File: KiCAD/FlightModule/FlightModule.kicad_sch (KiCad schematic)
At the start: 1 part, among them U1 ARDUINO_MKR_WAN_1310

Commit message: 本日の進捗をコミット
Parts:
- added Q1, Q2: AO3400A, Package_TO_SOT_SMD:SOT-23, symbol Transistor_FET:AO3400A
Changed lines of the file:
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@@
 	(paper "A4")
+	(symbol
+		(lib_id "Transistor_FET:AO3400A")
+		(at 167.64 40.64 0)
+		(unit 1)
+		(exclude_from_sim no)
+		(in_bom yes)
+		(on_board yes)
+		(dnp no)
+		(fields_autoplaced yes)
+		(property "Reference" "Q2"
+			(at 173.99 39.3699 0)
+			(effects
+				(font
+					(size 1.27 1.27)
+				)
+				(justify left)
+			)
+		)
+		(property "Value" "AO3400A"
+			(at 173.99 41.9099 0)
+			(effects
+				(font
+					(size 1.27 1.27)
+				)
+				(justify left)
+			)
+		)
+		(property "Footprint" "Package_TO_SOT_SMD:SOT-23"
+			(at 172.72 42.545 0)
+			(effects
+				(font
+					(size 1.27 1.27)
+					(italic yes)
+				)
+				(justify left)
+				(hide yes)
+			)
+		)
+		(property "Datasheet" "http://www.aosmd.com/pdfs/datasheet/AO3400A.pdf"
+			(at 172.72 44.45 0)
+			(effects
+				(font
+					(size 1.27 1.27)
+				)
+				(justify left)
+				(hide yes)
+			)
+		)
+		(property "Description" "30V Vds, 5.7A Id, N-Channel MOSFET, SOT-23"
+			(at 167.64 40.64 0)
+			(effects
+				(font
+					(size 1.27 1.27)
+				)
+				(hide yes)
+			)
+		)
+		(pin "1"
+		)
+		(pin "3"
+		)
+		(pin "2"
+		)
+		(instances
+			(project ""
+				(path "/3507137a-fdd7-4bc0-abe8-370b7c3b390e"
+					(reference "Q2")
+					(unit 1)
+				)
+			)
+		)
+	)
 	(symbol
 		(lib_id "ARDUINO_MKR_WAN_1310:ARDUINO_MKR_WAN_1310")
@@
 					(unit 1)
 				)
+			)
+		)
+	)
+	(symbol
+		(lib_id "Transistor_FET:AO3400A")
+		(at 166.37 63.5 0)
+		(unit 1)
+		(exclude_from_sim no)
+		(in_bom yes)
+		(on_board yes)
+		(dnp no)
+		(fields_autoplaced yes)
+		(property "Reference" "Q1"
+			(at 172.72 62.2299 0)
+			(effects
+				(font
+					(size 1.27 1.27)
+				)
+				(justify left)
+			)
+		)
+		(property "Value" "AO3400A"
+			(at 172.72 64.7699 0)
+			(effects
+				(font
+					(size 1.27 1.27)
+				)
+				(justify left)
+			)
+		)
+		(property "Footprint" "Package_TO_SOT_SMD:SOT-23"
+			(at 171.45 65.405 0)
+			(effects
+				(font
+					(size 1.27 1.27)
+					(italic yes)
+				)
+				(justify left)
+				(hide yes)
+			)
+		)
+		(property "Datasheet" "http://www.aosmd.com/pdfs/datasheet/AO3400A.pdf"
+			(at 171.45 67.31 0)
+			(effects
+				(font
+					(size 1.27 1.27)
+				)
+				(justify left)
+				(hide yes)
+			)
+		)
+		(property "Description" "30V Vds, 5.7A Id, N-Channel MOSFET, SOT-23"
+			(at 166.37 63.5 0)
+			(effects
+				(font
+					(size 1.27 1.27)
+				)
+				(hide yes)
+			)
+		)
+		(pin "3"
+		)
+		(pin "1"
+		)
+		(pin "2"
+		)
+		(instances
+			(project ""
+				(path "/3507137a-fdd7-4bc0-abe8-370b7c3b390e"
+					(reference "Q1")
+					(unit 1)
+				)

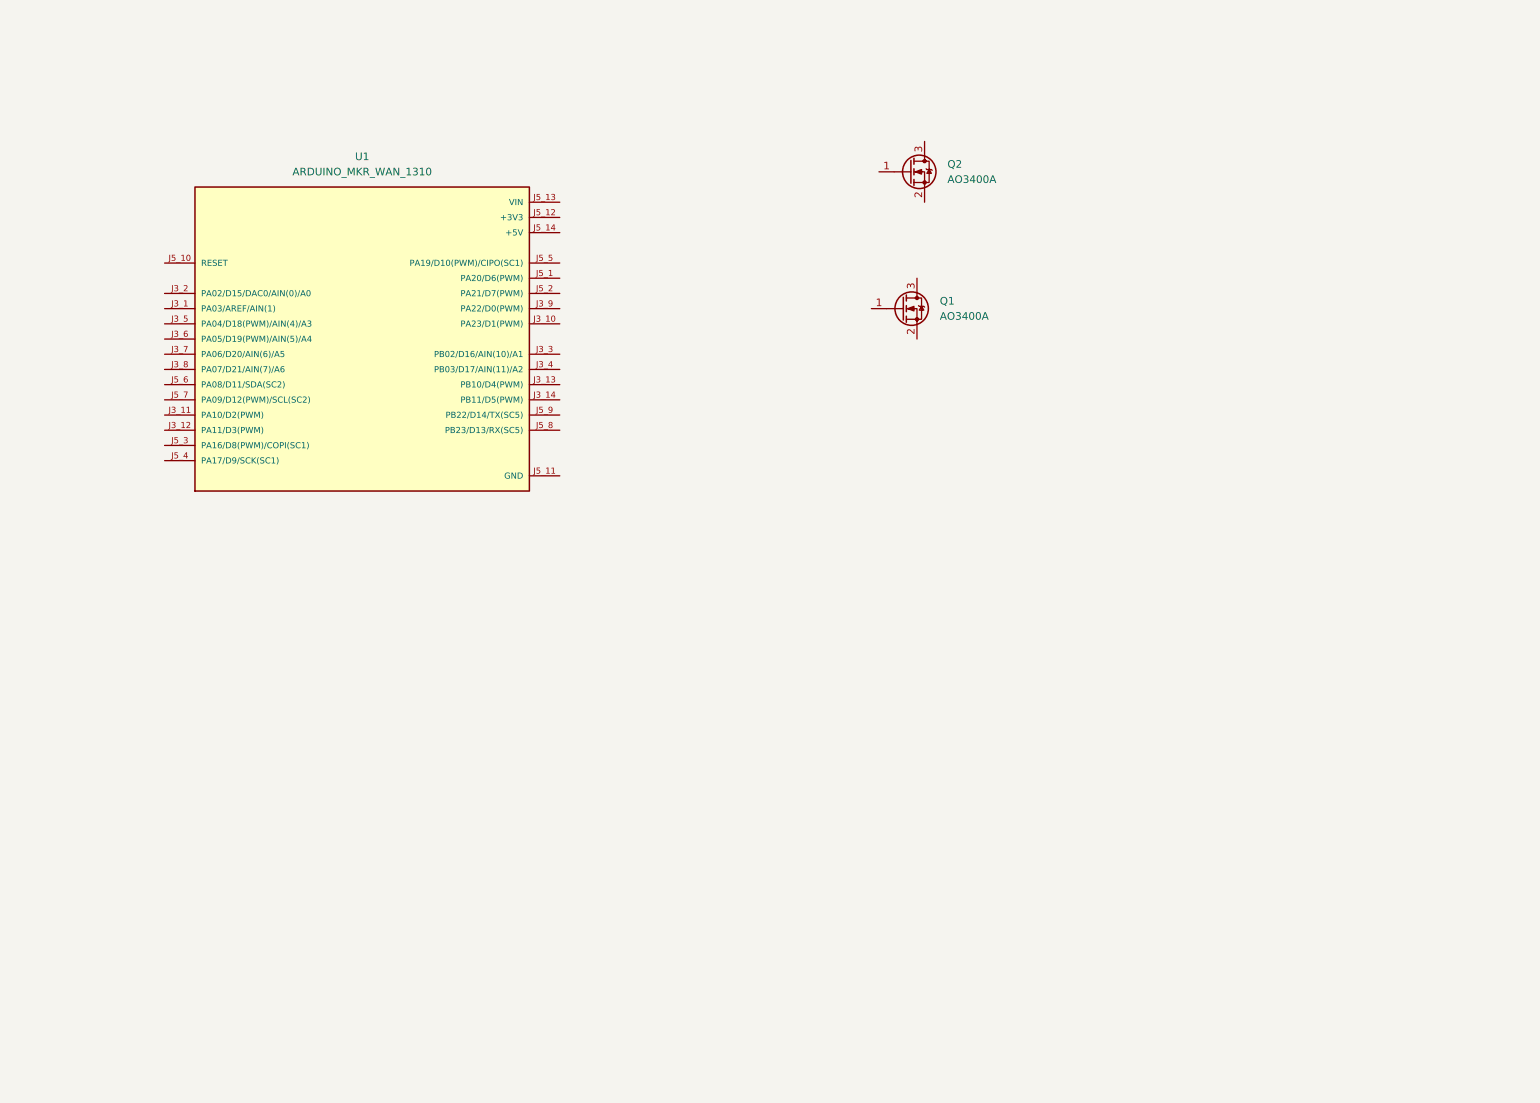
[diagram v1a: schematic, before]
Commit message: MB85RQ8MXを追加
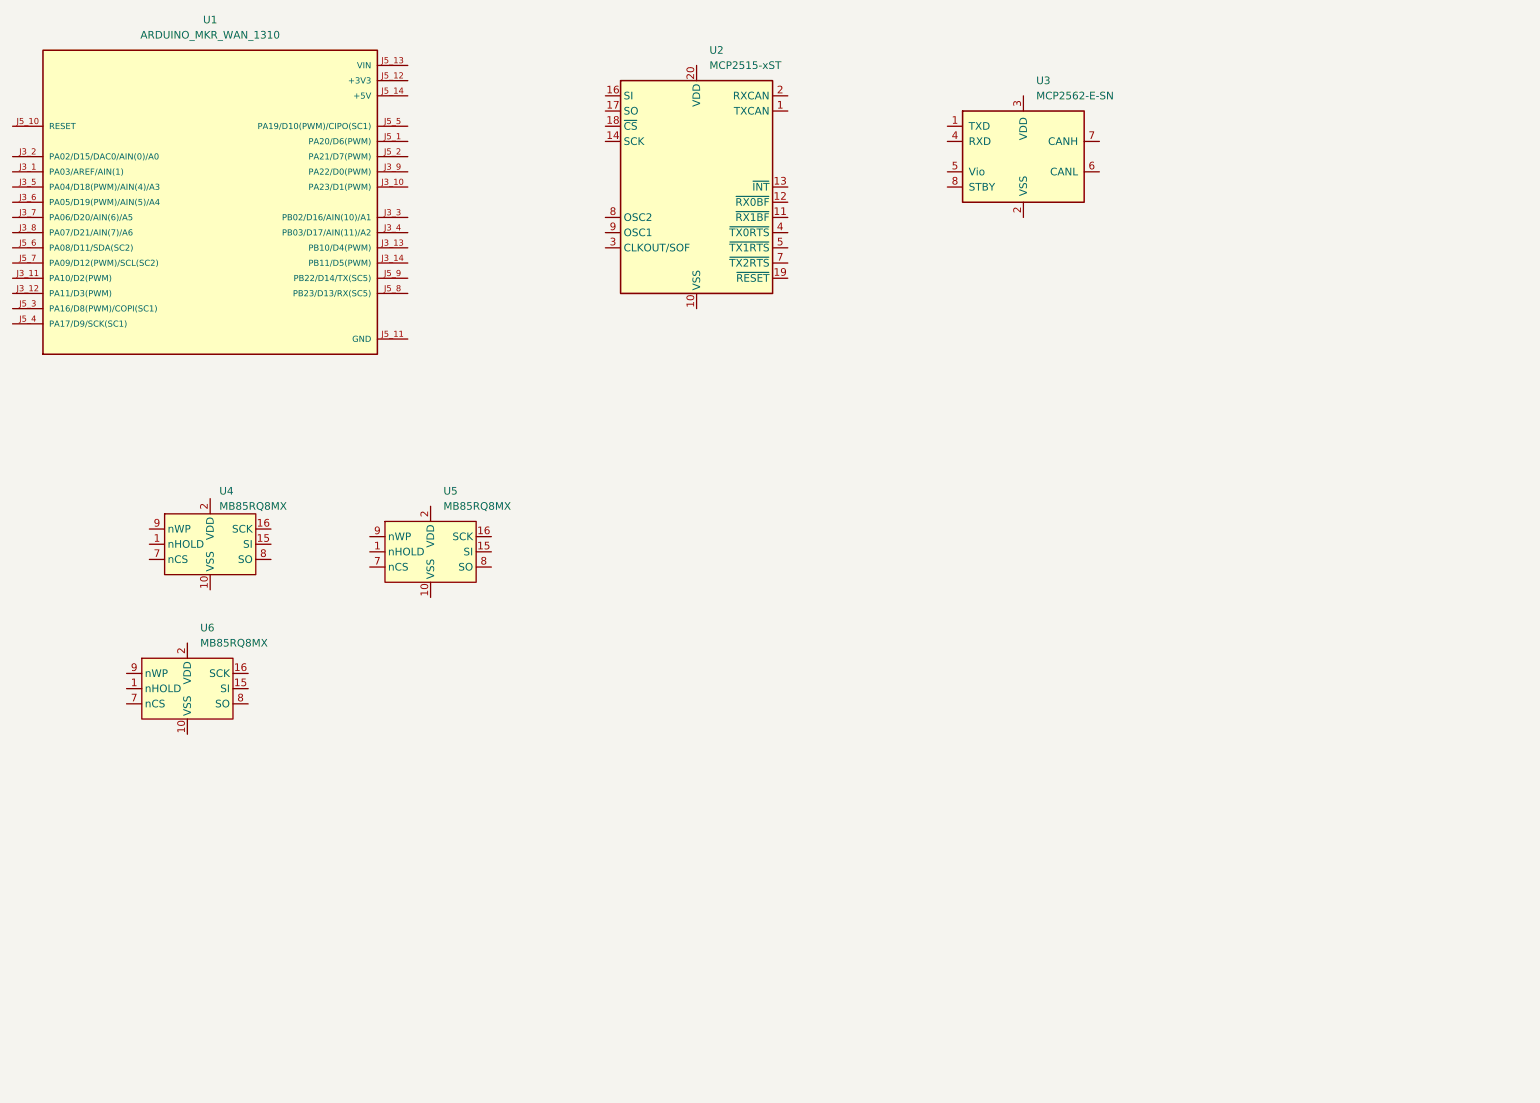
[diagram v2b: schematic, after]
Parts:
- removed Q1, Q2: AO3400A, Package_TO_SOT_SMD:SOT-23, symbol Transistor_FET:AO3400A
- added U2: MCP2515-xST, Package_SO:TSSOP-20_4.4x6.5mm_P0.65mm, symbol Interface_CAN_LIN:MCP2515-xST
- added U3: MCP2562-E-SN, Package_SO:SOIC-8_3.9x4.9mm_P1.27mm, symbol Interface_CAN_LIN:MCP2562-E-SN
- added U4: MB85RQ8MX, Package_SO:SOIC-16W_7.5x10.3mm_P1.27mm, symbol Memory_NVRAM:MB85RQ8MX
- added U5, U6: MB85RQ8MX, Package_SO:SOIC-16W_7.5x10.3mm_P1.27mm, symbol TSRP_IC:MB85RQ8MX

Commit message: 本日の進捗を保存
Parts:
- added U7: 74AHC1G14, symbol 74xGxx:74AHC1G14
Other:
- moved on the sheet: U4, U5, U6
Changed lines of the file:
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@@
 	(symbol
 		(lib_id "Memory_NVRAM:MB85RQ8MX")
-		(at 43.18 97.79 0)
+		(at 29.21 80.01 0)
 		(unit 1)
 		(exclude_from_sim no)
@@
 		(dnp no)
 		(property "Reference" "U4"
-			(at 52.324 93.98 0)
+			(at 38.354 76.2 0)
 			(effects
 				(font
@@
 		)
 		(property "Value" "MB85RQ8MX"
-			(at 52.324 96.52 0)
+			(at 38.354 78.74 0)
 			(effects
 				(font
@@
 		)
 		(property "Footprint" "Package_SO:SOIC-16W_7.5x10.3mm_P1.27mm"
-			(at 43.18 96.266 0)
+			(at 29.21 78.486 0)
 			(effects
 				(font
@@
 		)
 		(property "Datasheet" ""
-			(at 43.18 96.266 0)
+			(at 29.21 78.486 0)
 			(effects
 				(font
@@
 		)
 		(property "Description" ""
-			(at 43.18 96.266 0)
+			(at 29.21 78.486 0)
 			(effects
 				(font
@@
 		)
 		(property "Sim.Device" ""
-			(at 43.18 97.79 0)
+			(at 29.21 80.01 0)
 			(effects
 				(font
@@
 		)
 		(property "Sim.Pins" ""
-			(at 43.18 97.79 0)
+			(at 29.21 80.01 0)
 			(effects
 				(font
@@
 	)
 	(symbol
+		(lib_id "74xGxx:74AHC1G14")
+		(at 82.55 92.71 0)
+		(unit 1)
+		(exclude_from_sim no)
+		(in_bom yes)
+		(on_board yes)
+		(dnp no)
+		(fields_autoplaced yes)
+		(property "Reference" "U7"
+			(at 95.25 86.2898 0)
+			(effects
+				(font
+					(size 1.27 1.27)
+				)
+			)
+		)
+		(property "Value" "74AHC1G14"
+			(at 95.25 88.8298 0)
+			(effects
+				(font
+					(size 1.27 1.27)
+				)
+			)
+		)
+		(property "Footprint" ""
+			(at 82.55 92.71 0)
+			(effects
+				(font
+					(size 1.27 1.27)
+				)
+				(hide yes)
+			)
+		)
+		(property "Datasheet" "https://www.ti.com/lit/ds/symlink/sn74lvc1g14.pdf"
+			(at 82.55 99.06 0)
+			(effects
+				(font
+					(size 1.27 1.27)
+				)
+				(justify left)
+				(hide yes)
+			)
+		)
+		(property "Description" "Single Schmitt NOT Gate, Low-Voltage CMOS"
+			(at 82.55 92.71 0)
+			(effects
+				(font
+					(size 1.27 1.27)
+				)
+				(hide yes)
+			)
+		)
+		(pin "2"
+		)
+		(pin "5"
+		)
+		(pin "1"
+		)
+		(pin "3"
+		)
+		(pin "4"
+		)
+		(instances
+			(project ""
+				(path "/3507137a-fdd7-4bc0-abe8-370b7c3b390e"
+					(reference "U7")
+					(unit 1)
+				)
+			)
+		)
+	)
+	(symbol
 		(lib_id "TSRP_IC:MB85RQ8MX")
-		(at 80.01 99.06 0)
+		(at 29.21 123.19 0)
 		(unit 1)
 		(exclude_from_sim no)
@@
 		(fields_autoplaced yes)
 		(property "Reference" "U5"
-			(at 89.7733 93.98 0)
+			(at 38.9733 118.11 0)
 			(effects
 				(font
@@
 		)
 		(property "Value" "MB85RQ8MX"
-			(at 89.7733 96.52 0)
+			(at 38.9733 120.65 0)
 			(effects
 				(font
@@
 		)
 		(property "Footprint" "Package_SO:SOIC-16W_7.5x10.3mm_P1.27mm"
-			(at 80.01 97.536 0)
+			(at 29.21 121.666 0)
 			(effects
 				(font
@@
 		)
 		(property "Datasheet" ""
-			(at 80.01 97.536 0)
+			(at 29.21 121.666 0)
 			(effects
 				(font
@@
 		)
 		(property "Description" ""
-			(at 80.01 97.536 0)
+			(at 29.21 121.666 0)
 			(effects
 				(font
@@
 		)
 		(property "Sim.Device" ""
-			(at 80.01 99.06 0)
+			(at 29.21 123.19 0)
 			(effects
 				(font
@@
 		)
 		(property "Sim.Pins" ""
-			(at 80.01 99.06 0)
+			(at 29.21 123.19 0)
 			(effects
 				(font
@@
 	(symbol
 		(lib_id "TSRP_IC:MB85RQ8MX")
-		(at 39.37 121.92 0)
+		(at 29.21 102.87 0)
 		(unit 1)
 		(exclude_from_sim no)
@@
 		(fields_autoplaced yes)
 		(property "Reference" "U6"
-			(at 49.1333 116.84 0)
+			(at 38.9733 97.79 0)
 			(effects
 				(font
@@
 		)
 		(property "Value" "MB85RQ8MX"
-			(at 49.1333 119.38 0)
+			(at 38.9733 100.33 0)
 			(effects
 				(font
@@
 		)
 		(property "Footprint" "Package_SO:SOIC-16W_7.5x10.3mm_P1.27mm"
-			(at 39.37 120.396 0)
+			(at 29.21 101.346 0)
 			(effects
 				(font
@@
 		)
 		(property "Datasheet" ""
-			(at 39.37 120.396 0)
+			(at 29.21 101.346 0)
 			(effects
 				(font
@@
 		)
 		(property "Description" ""
-			(at 39.37 120.396 0)
+			(at 29.21 101.346 0)
 			(effects
 				(font
@@
 		)
 		(property "Sim.Device" ""
-			(at 39.37 121.92 0)
+			(at 29.21 102.87 0)
 			(effects
 				(font
@@
 		)
 		(property "Sim.Pins" ""
-			(at 39.37 121.92 0)
-			(effects
-				(font
+			(at 29.21 102.87 0)
+			(effects
+				(font

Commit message: 大型の部品を配置
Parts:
- added D1, D3: G, LED_SMD:LED_0603_1608Metric_Pad1.05x0.95mm_HandSolder, symbol Device:LED_Small
- added D2, D4: GS1010FL, Diode_SMD:D_SOD-123F, symbol Device:D_Small
- added Q1, Q2: AO3400A, Package_TO_SOT_SMD:SOT-23, symbol Transistor_FET:AO3400A
- added R1, R4: 300R, Resistor_SMD:R_0603_1608Metric_Pad0.98x0.95mm_HandSolder, symbol Device:R_Small
- added R2, R5: 10kR, Resistor_SMD:R_0603_1608Metric_Pad0.98x0.95mm_HandSolder, symbol Device:R_Small
- added R3, R6: 2.4kR, Resistor_SMD:R_0603_1608Metric_Pad0.98x0.95mm_HandSolder, symbol Device:R_Small
- added U8: L7805, symbol Regulator_Linear:L7805
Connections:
- new net: D3.1 (K), D4.2 (A), Q2.3 (D)
- new net: D3.2 (A), R6.2
- new net: Q1.1 (G), R1.2, R2.2
- new net: Q2.1 (G), R4.2, R5.2
- new net: D1.2 (A), R3.2
- new net: D1.1 (K), D2.2 (A), Q1.3 (D)
- new net +12V: D2.1 (K), D4.1 (K), R3.1, R6.1
- new net GND: Q1.2 (S), Q2.2 (S), R2.1, R5.1

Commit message: GPSSheildのフットプリントを救出
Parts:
- added IC1: ~, MKRGPSShield_V4.0:UBLOXLIB_SAM-M8Q, symbol MKRGPSShield_V4.0-eagle-import:SAM-M8Q
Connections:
- new net: IC1.1 (GND), IC1.10 (GND), IC1.11 (GND), IC1.15 (GND), IC1.16 (GND), IC1.20 (GND), IC1.4 (GND), IC1.5 (GND), IC1.6 (GND)
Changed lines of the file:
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@@
+	)
+	(symbol
+		(lib_id "MKRGPSShield_V4.0-eagle-import:SAM-M8Q")
+		(at 82.55 154.94 0)
+		(unit 1)
+		(exclude_from_sim no)
+		(in_bom yes)
+		(on_board yes)
+		(dnp no)
+		(fields_autoplaced yes)
+		(property "Reference" "IC1"
+			(at 82.55 154.94 0)
+			(effects
+				(font
+					(size 1.27 1.27)
+				)
+				(hide yes)
+			)
+		)
+		(property "Value" "~"
+			(at 82.55 154.94 0)
+			(effects
+				(font
+					(size 1.27 1.27)
+				)
+				(hide yes)
+			)
+		)
+		(property "Footprint" "MKRGPSShield_V4.0:UBLOXLIB_SAM-M8Q"
+			(at 82.55 154.94 0)
+			(effects
+				(font
+					(size 1.27 1.27)
+				)
+				(hide yes)
+			)
+		)
+		(property "Datasheet" ""
+			(at 82.55 154.94 0)
+			(effects
+				(font
+					(size 1.27 1.27)
+				)
+				(hide yes)
+			)
+		)
+		(property "Description" "u-blox SAM GNSS antenna module"
+			(at 82.55 154.94 0)
+			(effects
+				(font
+					(size 1.27 1.27)
+				)
+				(hide yes)
+			)
+		)
+		(pin "14"
+		)
+		(pin "13"
+		)
+		(pin "8"
+		)
+		(pin "17"
+		)
+		(pin "9"
+		)
+		(pin "12"
+		)
+		(pin "19"
+		)
+		(pin "7"
+		)
+		(pin "18"
+		)
+		(pin "2"
+		)
+		(pin "3"
+		)
+		(pin "1"
+		)
+		(pin "10"
+		)
+		(pin "11"
+		)
+		(pin "15"
+		)
+		(pin "16"
+		)
+		(pin "20"
+		)
+		(pin "4"
+		)
+		(pin "5"
+		)
+		(pin "6"
+		)
+		(instances
+			(project ""
+				(path "/3507137a-fdd7-4bc0-abe8-370b7c3b390e"
+					(reference "IC1")
+					(unit 1)
+				)
+			)
+		)
 	)
 	(symbol

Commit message: GPSShieldのフットプリントをFlightModuleに移植（手作業☠️）
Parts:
- IC1: footprint MKRGPSShield_V4.0:UBLOXLIB_SAM-M8Q -> GPSShield:UBLOXLIB_SAM-M8Q
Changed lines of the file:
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@@
+	)
+	(symbol
+		(lib_id "MKRGPSShield_V4.0-eagle-import:SAM-M8Q")
+		(at 81.28 162.56 0)
+		(unit 1)
+		(exclude_from_sim no)
+		(in_bom yes)
+		(on_board yes)
+		(dnp no)
+		(fields_autoplaced yes)
+		(property "Reference" "IC1"
+			(at 81.28 162.56 0)
+			(effects
+				(font
+					(size 1.27 1.27)
+				)
+				(hide yes)
+			)
+		)
+		(property "Value" "~"
+			(at 81.28 162.56 0)
+			(effects
+				(font
+					(size 1.27 1.27)
+				)
+				(hide yes)
+			)
+		)
+		(property "Footprint" "GPSShield:UBLOXLIB_SAM-M8Q"
+			(at 81.28 162.56 0)
+			(effects
+				(font
+					(size 1.27 1.27)
+				)
+				(hide yes)
+			)
+		)
+		(property "Datasheet" ""
+			(at 81.28 162.56 0)
+			(effects
+				(font
+					(size 1.27 1.27)
+				)
+				(hide yes)
+			)
+		)
+		(property "Description" "u-blox SAM GNSS antenna module"
+			(at 81.28 162.56 0)
+			(effects
+				(font
+					(size 1.27 1.27)
+				)
+				(hide yes)
+			)
+		)
+		(pin "11"
+		)
+		(pin "2"
+		)
+		(pin "15"
+		)
+		(pin "1"
+		)
+		(pin "3"
+		)
+		(pin "10"
+		)
+		(pin "8"
+		)
+		(pin "18"
+		)
+		(pin "16"
+		)
+		(pin "7"
+		)
+		(pin "5"
+		)
+		(pin "20"
+		)
+		(pin "19"
+		)
+		(pin "4"
+		)
+		(pin "6"
+		)
+		(pin "12"
+		)
+		(pin "13"
+		)
+		(pin "14"
+		)
+		(pin "17"
+		)
+		(pin "9"
+		)
+		(instances
+			(project ""
+				(path "/3507137a-fdd7-4bc0-abe8-370b7c3b390e"
+					(reference "IC1")
+					(unit 1)
+				)
+			)
+		)
 	)
 	(symbol
@@
 					(unit 1)
 				)
-			)
-		)
-	)
-	(symbol
-		(lib_id "MKRGPSShield_V4.0-eagle-import:SAM-M8Q")
-		(at 82.55 154.94 0)
-		(unit 1)
-		(exclude_from_sim no)
-		(in_bom yes)
-		(on_board yes)
-		(dnp no)
-		(fields_autoplaced yes)
-		(property "Reference" "IC1"
-			(at 82.55 154.94 0)
-			(effects
-				(font
-					(size 1.27 1.27)
-				)
-				(hide yes)
-			)
-		)
-		(property "Value" "~"
-			(at 82.55 154.94 0)
-			(effects
-				(font
-					(size 1.27 1.27)
-				)
-				(hide yes)
-			)
-		)
-		(property "Footprint" "MKRGPSShield_V4.0:UBLOXLIB_SAM-M8Q"
-			(at 82.55 154.94 0)
-			(effects
-				(font
-					(size 1.27 1.27)
-				)
-				(hide yes)
-			)
-		)
-		(property "Datasheet" ""
-			(at 82.55 154.94 0)
-			(effects
-				(font
-					(size 1.27 1.27)
-				)
-				(hide yes)
-			)
-		)
-		(property "Description" "u-blox SAM GNSS antenna module"
-			(at 82.55 154.94 0)
-			(effects
-				(font
-					(size 1.27 1.27)
-				)
-				(hide yes)
-			)
-		)
-		(pin "14"
-		)
-		(pin "13"
-		)
-		(pin "8"
-		)
-		(pin "17"
-		)
-		(pin "9"
-		)
-		(pin "12"
-		)
-		(pin "19"
-		)
-		(pin "7"
-		)
-		(pin "18"
-		)
-		(pin "2"
-		)
-		(pin "3"
-		)
-		(pin "1"
-		)
-		(pin "10"
-		)
-		(pin "11"
-		)
-		(pin "15"
-		)
-		(pin "16"
-		)
-		(pin "20"
-		)
-		(pin "4"
-		)
-		(pin "5"
-		)
-		(pin "6"
-		)
-		(instances
-			(project ""
-				(path "/3507137a-fdd7-4bc0-abe8-370b7c3b390e"
-					(reference "IC1")
-					(unit 1)
-				)

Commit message: GPSShieldの配線の再現の途中
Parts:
- added U9: ~, MKRGPSShield_V4.0:SOT25, symbol MKRGPSShield_V4.0-eagle-import:AP2112K-3.3
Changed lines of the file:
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@@
+	)
+	(symbol
+		(lib_id "MKRGPSShield_V4.0-eagle-import:AP2112K-3.3")
+		(at 149.86 143.51 0)
+		(unit 1)
+		(exclude_from_sim no)
+		(in_bom yes)
+		(on_board yes)
+		(dnp no)
+		(fields_autoplaced yes)
+		(property "Reference" "U9"
+			(at 149.86 134.62 0)
+			(effects
+				(font
+					(size 1.778 1.5113)
+				)
+			)
+		)
+		(property "Value" "~"
+			(at 149.86 137.16 0)
+			(effects
+				(font
+					(size 1.778 1.5113)
+				)
+			)
+		)
+		(property "Footprint" "MKRGPSShield_V4.0:SOT25"
+			(at 149.86 143.51 0)
+			(effects
+				(font
+					(size 1.27 1.27)
+				)
+				(hide yes)
+			)
+		)
+		(property "Datasheet" ""
+			(at 149.86 143.51 0)
+			(effects
+				(font
+					(size 1.27 1.27)
+				)
+				(hide yes)
+			)
+		)
+		(property "Description" "IC REG LINEAR 3.3V 600mA SOT25"
+			(at 149.86 143.51 0)
+			(effects
+				(font
+					(size 1.27 1.27)
+				)
+				(hide yes)
+			)
+		)
+		(pin "1"
+		)
+		(pin "3"
+		)
+		(pin "2"
+		)
+		(pin "5"
+		)
+		(instances
+			(project ""
+				(path "/3507137a-fdd7-4bc0-abe8-370b7c3b390e"
+					(reference "U9")
+					(unit 1)
+				)
+			)
+		)
 	)
 	(symbol
